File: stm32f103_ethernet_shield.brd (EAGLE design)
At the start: 85.1 x 75.9 mm, 6 parts

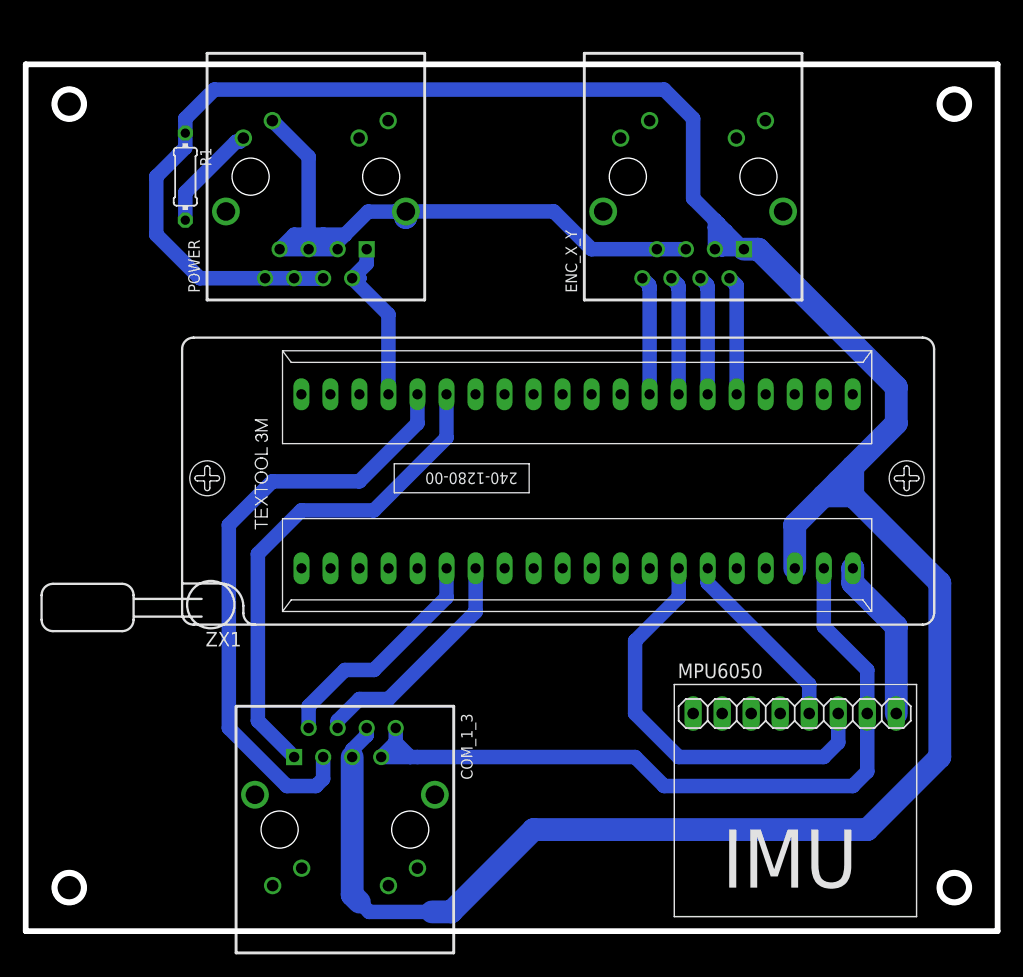
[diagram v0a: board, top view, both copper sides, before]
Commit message: Removed old backups
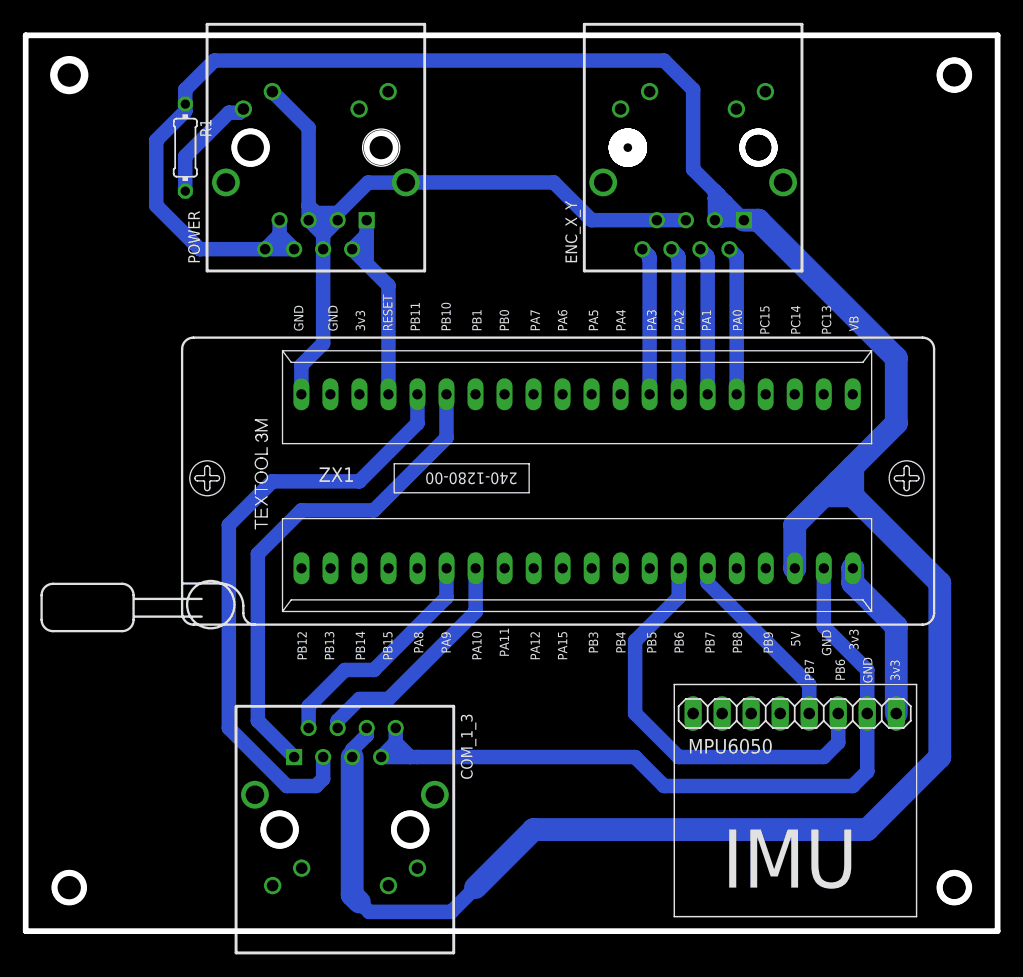
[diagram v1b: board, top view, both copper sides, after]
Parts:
- moved ENC_X_Y 2.54 mm to (58.4, 68.6)
- moved POWER 2.54 mm to (25.4, 68.6)
- moved R1 2.54 mm to (14.0, 68.6)
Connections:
- net 5V: now also POWER.7; no longer POWER.4
- net GND@3: now also POWER.4; no longer POWER.7
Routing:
- net GND@3: track 59.8 -> 69.9 mm
- net RESET: track 15.8 -> 19.6 mm
- net PA_3: track 10.4 -> 13.0 mm
- net PA_2: track 10.4 -> 13.0 mm
- net PA_1: track 10.4 -> 13.0 mm
- net PA_0: track 10.4 -> 13.0 mm
- net 5V: track 240.6 -> 242.9 mm
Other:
- board size 85.1 x 75.9 mm -> 85.1 x 78.4 mm
- board text added: "3v3"
- board text added: "5V"
- board text added: "GND"
- board text added: "PA0"
- board text added: "PA1"
- board text added: "PA10"
- board text added: "PA11"
- board text added: "PA12"
- board text added: "PA15"
- board text added: "PA2"
- board text added: "PA3"
- board text added: "PA4"
- board text added: "PA5"
- board text added: "PA6"
- board text added: "PA7"
- board text added: "PA8"
- board text added: "PA9"
- board text added: "PB0"
- board text added: "PB1"
- board text added: "PB10"
- board text added: "PB11"
- board text added: "PB12"
- board text added: "PB13"
- board text added: "PB14"
- board text added: "PB15"
- board text added: "PB3"
- board text added: "PB4"
- board text added: "PB5"
- board text added: "PB6"
- board text added: "PB7"
- board text added: "PB8"
- board text added: "PB9"
- board text added: "PC13"
- board text added: "PC14"
- board text added: "PC15"
- board text added: "RESET"
- board text added: "VB"
